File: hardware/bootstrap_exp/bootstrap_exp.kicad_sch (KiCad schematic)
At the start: 27 parts, among them J1 Conn_Coaxial, J2 Conn_Coaxial, U1 OPA810DBV, U2 OPA810DBV, U3 OPA810DBV

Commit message: Assign names to nets
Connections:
- net FRONT_OUT: now reaches R2.1, TP5.1, U1.1, U1.4 (-), U3.3 (+)
- net FRONT_IN: now reaches C1.1, R4.1, U1.3 (+)
- net BOOT: now reaches R4.2, R5.1, R6.1
- net BOOT_DIV: now reaches R2.2, R3.1, R5.2, U2.3 (+)
- net BOOT_BUF: now reaches R6.2, TP6.1, U2.1, U2.4 (-)
- net AMP_OUT: now reaches R7.1, TP7.1, U3.1, U3.4 (-)
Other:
- moved on the sheet: J2, R7
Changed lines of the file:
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@@
     (stroke (width 0) (type default) (color 0 0 0 0))
   )
-  (wire (pts (xy 205.74 63.5) (xy 208.28 63.5))
+  (wire (pts (xy 204.47 63.5) (xy 207.01 63.5))
     (stroke (width 0) (type default) (color 0 0 0 0))
   )
@@
     (stroke (width 0) (type default) (color 0 0 0 0))
   )
-  (wire (pts (xy 193.04 63.5) (xy 198.12 63.5))
+  (wire (pts (xy 193.04 63.5) (xy 196.85 63.5))
     (stroke (width 0) (type default) (color 0 0 0 0))
   )
@@
     (stroke (width 0) (type default) (color 0 0 0 0))
   )
-  (wire (pts (xy 213.36 68.58) (xy 213.36 71.12))
+  (wire (pts (xy 212.09 68.58) (xy 212.09 71.12))
     (stroke (width 0) (type default) (color 0 0 0 0))
   )
@@
   (wire (pts (xy 127 53.34) (xy 127 50.8))
     (stroke (width 0) (type default) (color 0 0 0 0))
+  )
+  (label "BOOT_DIV" (at 120.65 83.82 0)
+    (effects (font (size 1.27 1.27)) (justify left bottom))
   )
   (label "V-" (at 167.64 132.08 180)
@@
     (effects (font (size 1.27 1.27)) (justify left bottom))
   )
+  (label "BOOT" (at 107.95 74.93 90)
+    (effects (font (size 1.27 1.27)) (justify left bottom))
+  )
+  (label "AMP_OUT" (at 177.8 76.2 0)
+    (effects (font (size 1.27 1.27)) (justify left bottom))
+  )
+  (label "BOOT_BUF" (at 129.54 113.03 0)
+    (effects (font (size 1.27 1.27)) (justify left bottom))
+  )
   (label "V-" (at 175.26 73.66 90)
     (effects (font (size 1.27 1.27)) (justify left bottom))
@@
   (label "V+" (at 175.26 53.34 270)
     (effects (font (size 1.27 1.27)) (justify right bottom))
+  )
+  (label "FRONT_IN" (at 110.49 58.42 0)
+    (effects (font (size 1.27 1.27)) (justify left bottom))
+  )
+  (label "FRONT_OUT" (at 128.27 73.66 0)
+    (effects (font (size 1.27 1.27)) (justify left bottom))
   )
   (symbol (lib_id "Device:R") (at 85.09 64.77 0) (unit 1)
@@
     (pin "1")
   )
-  (symbol (lib_id "Connector:Conn_Coaxial") (at 213.36 63.5 0) (unit 1)
-    (in_bom yes) (on_board yes) (fields_autoplaced)
-    (property "Reference" "J2" (id 0) (at 213.0426 55.88 0))
-    (property "Value" "Conn_Coaxial" (id 1) (at 213.0426 58.42 0))
-    (property "Footprint" "Connector_Coaxial:SMA_Samtec_SMA-J-P-X-ST-EM1_EdgeMount" (id 2) (at 213.36 63.5 0)
-      (effects (font (size 1.27 1.27)) hide)
-    )
-    (property "Datasheet" " ~" (id 3) (at 213.36 63.5 0)
+  (symbol (lib_id "Connector:Conn_Coaxial") (at 212.09 63.5 0) (unit 1)
+    (in_bom yes) (on_board yes) (fields_autoplaced)
+    (property "Reference" "J2" (id 0) (at 211.7726 55.88 0))
+    (property "Value" "Conn_Coaxial" (id 1) (at 211.7726 58.42 0))
+    (property "Footprint" "Connector_Coaxial:SMA_Samtec_SMA-J-P-X-ST-EM1_EdgeMount" (id 2) (at 212.09 63.5 0)
+      (effects (font (size 1.27 1.27)) hide)
+    )
+    (property "Datasheet" " ~" (id 3) (at 212.09 63.5 0)
       (effects (font (size 1.27 1.27)) hide)
     )
@@
     (pin "1")
   )
-  (symbol (lib_id "power:GND") (at 213.36 71.12 0) (mirror y) (unit 1)
-    (in_bom yes) (on_board yes) (fields_autoplaced)
-    (property "Reference" "#PWR08" (id 0) (at 213.36 77.47 0)
-      (effects (font (size 1.27 1.27)) hide)
-    )
-    (property "Value" "GND" (id 1) (at 213.36 76.2 0))
-    (property "Footprint" "" (id 2) (at 213.36 71.12 0)
-      (effects (font (size 1.27 1.27)) hide)
-    )
-    (property "Datasheet" "" (id 3) (at 213.36 71.12 0)
+  (symbol (lib_id "power:GND") (at 212.09 71.12 0) (mirror y) (unit 1)
+    (in_bom yes) (on_board yes) (fields_autoplaced)
+    (property "Reference" "#PWR08" (id 0) (at 212.09 77.47 0)
+      (effects (font (size 1.27 1.27)) hide)
+    )
+    (property "Value" "GND" (id 1) (at 212.09 76.2 0))
+    (property "Footprint" "" (id 2) (at 212.09 71.12 0)
+      (effects (font (size 1.27 1.27)) hide)
+    )
+    (property "Datasheet" "" (id 3) (at 212.09 71.12 0)
       (effects (font (size 1.27 1.27)) hide)
     )
@@
     (pin "2")
   )
-  (symbol (lib_id "Device:R") (at 201.93 63.5 90) (unit 1)
-    (in_bom yes) (on_board yes) (fields_autoplaced)
-    (property "Reference" "R7" (id 0) (at 201.93 57.15 90))
-    (property "Value" "50" (id 1) (at 201.93 59.69 90))
-    (property "Footprint" "Resistor_SMD:R_0603_1608Metric" (id 2) (at 201.93 65.278 90)
-      (effects (font (size 1.27 1.27)) hide)
-    )
-    (property "Datasheet" "~" (id 3) (at 201.93 63.5 0)
-      (effects (font (size 1.27 1.27)) hide)
-    )
+  (symbol (lib_id "Device:R") (at 200.66 63.5 90) (unit 1)
+    (in_bom yes) (on_board yes) (fields_autoplaced)
+    (property "Reference" "R7" (id 0) (at 200.66 57.15 90))
+    (property "Value" "50" (id 1) (at 200.66 59.69 90))
+    (property "Footprint" "Resistor_SMD:R_0603_1608Metric" (id 2) (at 200.66 65.278 90)
+      (effects (font (size 1.27 1.27)) hide)
+    )
+    (property "Datasheet" "~" (id 3) (at 200.66 63.5 0)
+      (effects (font (size 1.27 1.27)) hide)
+    )

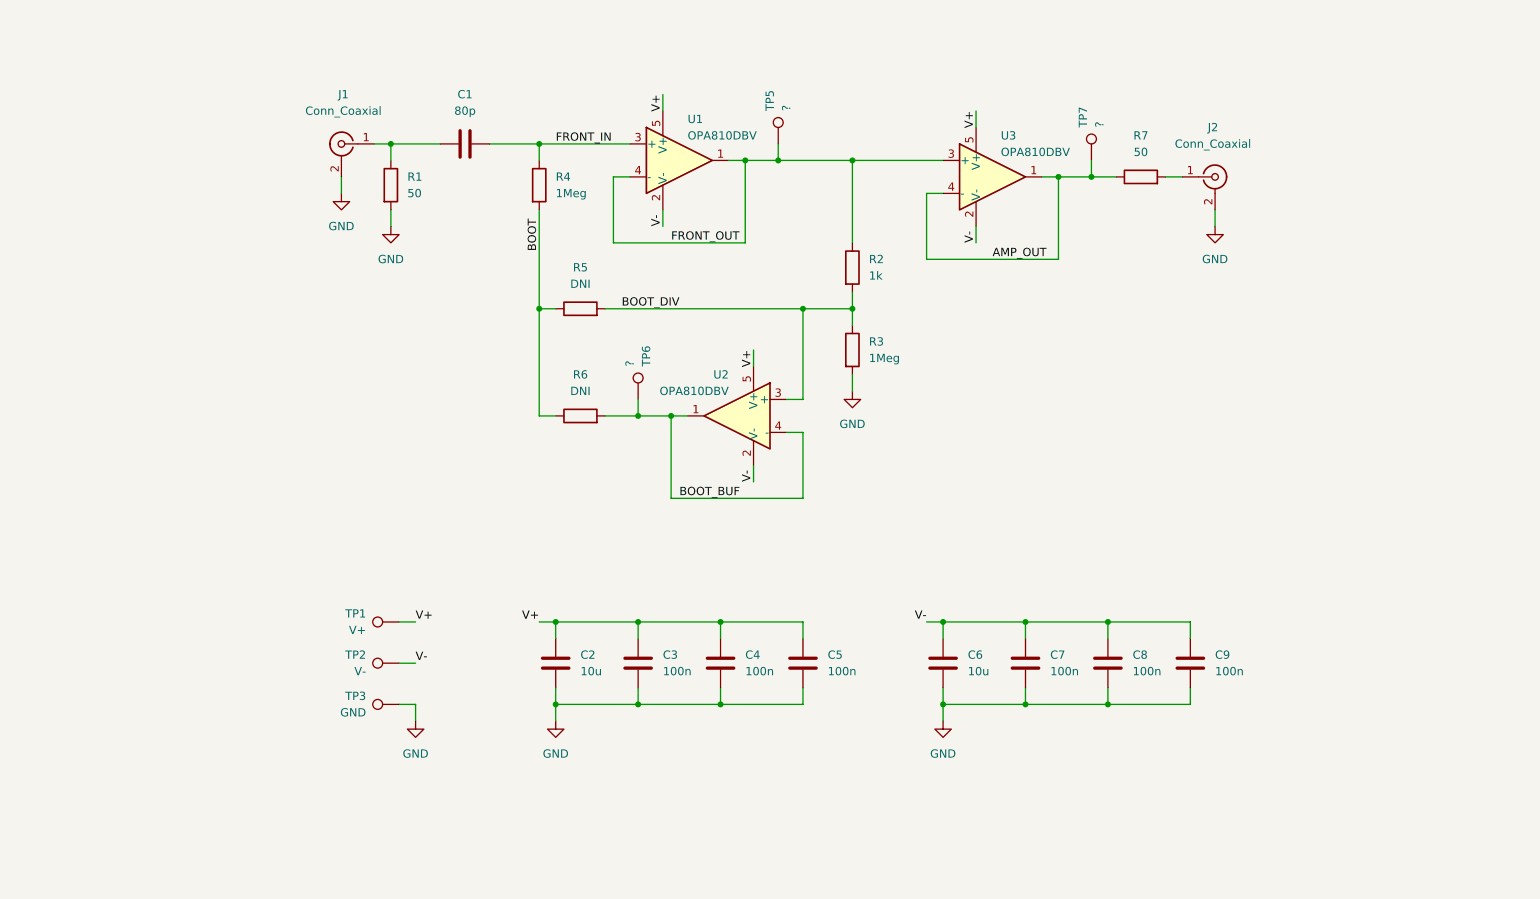
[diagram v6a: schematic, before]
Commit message: Add input buffer
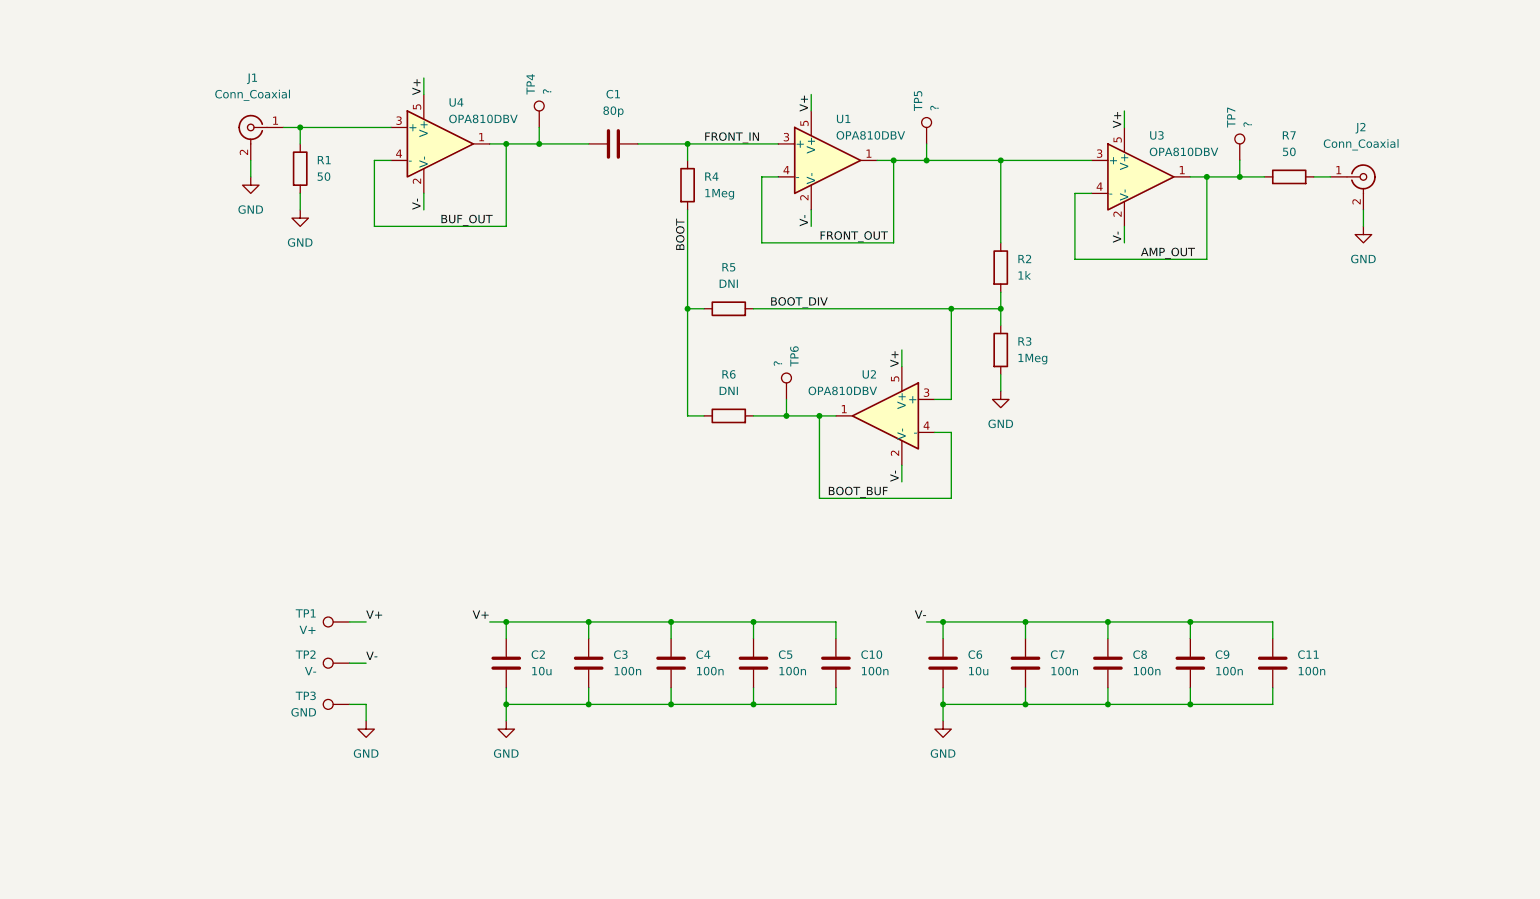
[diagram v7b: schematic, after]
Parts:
- added C10, C11: 100n, Capacitor_SMD:C_0603_1608Metric, symbol Device:C
- added TP4: ?, TestPoint:TestPoint_Keystone_5005-5009_Compact, symbol Connector:TestPoint
- added U4: OPA810DBV, Package_TO_SOT_SMD:SOT-23-5, symbol local_symbols:OPA810DBV
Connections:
- net GND: now also C10.2, C11.2
- net V+: now also C10.1, U4.5 (V+)
- net V-: now also C11.1, U4.2 (V-)
- net at J1.1 (In), R1.1: now also U4.3 (+); no longer C1.2
- new net BUF_OUT: C1.2, TP4.1, U4.1, U4.4 (-)
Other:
- moved on the sheet: C1, C2, C3, C4, C5, J1, J2, R1, R2, R3, R4, R5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

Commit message: Finish routing
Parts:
- added TP?: GND, TestPoint:TestPoint_Keystone_5005-5009_Compact, symbol Connector:TestPoint
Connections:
- net GND: now also TP?.1
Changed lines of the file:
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@@
+    (stroke (width 0) (type default) (color 0 0 0 0))
+  )
+  (wire (pts (xy 67.31 87.63) (xy 69.85 87.63))
     (stroke (width 0) (type default) (color 0 0 0 0))
   )
@@
   )
   (wire (pts (xy 115.57 132.08) (xy 115.57 134.62))
+    (stroke (width 0) (type default) (color 0 0 0 0))
+  )
+  (wire (pts (xy 69.85 87.63) (xy 69.85 90.17))
     (stroke (width 0) (type default) (color 0 0 0 0))
   )
@@
     (pin "1")
   )
+  (symbol (lib_id "power:GND") (at 69.85 90.17 0) (unit 1)
+    (in_bom yes) (on_board yes) (fields_autoplaced)
+    (property "Reference" "#PWR?" (id 0) (at 69.85 96.52 0)
+      (effects (font (size 1.27 1.27)) hide)
+    )
+    (property "Value" "GND" (id 1) (at 69.85 95.25 0))
+    (property "Footprint" "" (id 2) (at 69.85 90.17 0)
+      (effects (font (size 1.27 1.27)) hide)
+    )
+    (property "Datasheet" "" (id 3) (at 69.85 90.17 0)
+      (effects (font (size 1.27 1.27)) hide)
+    )
+    (pin "1")
+  )
   (symbol (lib_id "Device:R") (at 130.81 64.77 0) (unit 1)
     (in_bom yes) (on_board yes) (fields_autoplaced)
@@
     (pin "4")
   )
+  (symbol (lib_id "Connector:TestPoint") (at 67.31 87.63 90) (mirror x) (unit 1)
+    (in_bom yes) (on_board yes)
+    (property "Reference" "TP?" (id 0) (at 62.23 86.36 90)
+      (effects (font (size 1.27 1.27)) (justify left))
+    )
+    (property "Value" "GND" (id 1) (at 62.23 88.9 90)
+      (effects (font (size 1.27 1.27)) (justify left))
+    )
+    (property "Footprint" "TestPoint:TestPoint_Keystone_5005-5009_Compact" (id 2) (at 67.31 92.71 0)
+      (effects (font (size 1.27 1.27)) hide)
+    )
+    (property "Datasheet" "~" (id 3) (at 67.31 92.71 0)
+      (effects (font (size 1.27 1.27)) hide)
+    )
+    (pin "1")
+  )
   (symbol (lib_id "local_symbols:OPA810DBV") (at 200.66 63.5 0) (unit 1)
     (in_bom yes) (on_board yes)
@@
       (reference "#PWR08") (unit 1) (value "GND") (footprint "")
     )
+    (path "/1f1f5a5e-93ba-4083-b840-ba05eefc4082"
+      (reference "#PWR?") (unit 1) (value "GND") (footprint "")
+    )
     (path "/a7d158f3-55a4-47ef-8947-cfce6892a922"
       (reference "C1") (unit 1) (value "80p") (footprint "Capacitor_SMD:C_0603_1608Metric")
@@
       (reference "TP7") (unit 1) (value "?") (footprint "TestPoint:TestPoint_Keystone_5005-5009_Compact")
     )
+    (path "/ebd243f0-1c55-483e-88ff-76d4cdd404f4"
+      (reference "TP?") (unit 1) (value "GND") (footprint "TestPoint:TestPoint_Keystone_5005-5009_Compact")
+    )
     (path "/de13541f-796c-4950-ab90-fb9467a8b0a3"
